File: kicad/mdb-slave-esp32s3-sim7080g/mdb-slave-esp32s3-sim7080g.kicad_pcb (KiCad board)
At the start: 2 copper layers, 58.4 x 41 mm, 56 parts, among them J1 MDB_Connector, J2 USB_C_Receptacle_USB2.0_16P, J3 Conn_02x11_Odd_Even, J4 JAE_SIM_Card_SF72S006, J5 Conn_Coaxial, J6 Conn_Coaxial, SW1 SW_Push, U1 TLP785, U2 SIM7080G, U3 ESP32-S3FH4R2, U4 TLP785, U5 LM2594HVM-3.3, Y1 Crystal_GND24

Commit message: UPdating references
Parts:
- removed AE2: Antenna, RF_Antenna:Johanson_2450AT43F0100
- removed the C4 at (180.2, 90.9)
- removed the D2 at (236.0, 107.1)
- removed the J6 at (240.5, 92.2)
- removed the R1 at (230.6, 110.5)
- added C1: 1.8pf, Capacitor_SMD:C_0603_1608Metric, F.Cu at (235.5, 119.6)
- added C2: NC, Capacitor_SMD:C_0603_1608Metric, F.Cu at (235.5, 122.1)
- added D3: LED, LED_SMD:LED_0603_1608Metric, F.Cu at (247.6, 128.8)
- added J5: Conn_Coaxial, Connector_Coaxial:U.FL_Hirose_U.FL-R-SMT-1_Vertical, F.Cu at (248.1, 121.4)
- added Q1: NPN, Package_TO_SOT_SMD:SOT-23, F.Cu at (231.1, 120.6)
- added Q2: NPN, Package_TO_SOT_SMD:SOT-23, F.Cu at (231.1, 125.0)
- added Q3: NPN, Package_TO_SOT_SMD:SOT-23, F.Cu at (231.1, 129.5)
- added R12: 22ohm, Resistor_SMD:R_0603_1608Metric, F.Cu at (243.6, 119.6)
- added R13: 22ohm, Resistor_SMD:R_0603_1608Metric, F.Cu at (243.6, 122.1)
- added R14: 22ohm, Resistor_SMD:R_0603_1608Metric, F.Cu at (243.6, 124.6)
- added R15: 1k, Resistor_SMD:R_0603_1608Metric, F.Cu at (243.6, 127.2)
- added R2: 10K, Resistor_SMD:R_0603_1608Metric, F.Cu at (239.5, 119.6)
- added R3: 10K, Resistor_SMD:R_0603_1608Metric, F.Cu at (239.5, 122.1)
- added R4: 4K7, Resistor_SMD:R_0603_1608Metric, F.Cu at (239.5, 124.6)
- added R5: 4K7, Resistor_SMD:R_0603_1608Metric, F.Cu at (239.5, 127.2)
- added R6: 4K7, Resistor_SMD:R_0603_1608Metric, F.Cu at (239.5, 129.7)
- added TP3: TestPoint, TestPoint:TestPoint_Pad_D1.0mm, F.Cu at (247.1, 125.9)
- C18: renamed from C19; value 1.8pf -> 27pf
- C19: renamed from C18; value 1.8pf -> 27pf
- C20: value 1.8pf -> NC
- C21: renamed from C17; value 1.8pf -> NC
- L3, L4: value 2.4nh -> 47nh
- moved L1 63.2 mm to (235.5, 124.6)
- moved L3 22.2 mm to (235.5, 127.2)
- moved L4 22.2 mm to (235.5, 129.7)
- moved AE1 0.42 mm to (180.6, 88.7)
- renumbered C7 to C10, C14 to C11, C16 to C12, C15 to C13, C12 to C14, C3 to C15, C13 to C16, C2 to C17, C1 to C3, C5 to C4, C6 to C5, C11 to C6, C8 to C7, C9 to C8, C10 to C9, D5 to D1, D4 to D2, D1 to D4, J2 to J1, J4 to J2, J5 to J4, J1 to J6, R3 to R1, R7 to R10, R8 to R11, R2 to R16, R10 to R17, R5 to R18, R9 to R7, R4 to R8, R6 to R9, TP4 to TP1, TP1 to TP2, U3 to U1, U5 to U3, U1 to U5
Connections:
- C18 pad 2: Net-(J5-In) -> Net-(J4-In)
- C19 pad 2: Net-(AE2-A) -> Net-(J5-In)
- J2 pad C2: /sim_rst -> Net-(J2-RST)
- J2 pad C3: /sim_clk -> Net-(J2-CLK)
- J2 pad C7: /sim_data -> Net-(J2-I/O)
- J4 pad 1: Net-(J5-In) -> Net-(J4-In)
- L1 pad 2: GND -> Net-(U1-LNA_IN/RF)
- L3 pad 1: Net-(AE2-A) -> Net-(J4-In)
- L3 pad 2: /rf_ant -> /gnss_ant
- L4 pad 2: /gnss_ant -> /rf_ant
- U1 pad 1: Net-(U3-LNA_IN/RF) -> Net-(U1-LNA_IN/RF)
- U2 pad 1: /io18 -> /sim_uart1_tx
- U2 pad 2: /io17 -> /sim_uart1_rx
- U2 pad 39: /io14 -> /pwrkey
- U2 pad 40: unconnected-(U2-VDD_EXT-Pad40) -> /sim_vdd_ext

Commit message: Initial organization
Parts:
- removed D3: LED, LED_SMD:LED_0603_1608Metric
- removed R15: 1k, Resistor_SMD:R_0603_1608Metric
- added TP4: TestPoint, TestPoint:TestPoint_Pad_D1.0mm, F.Cu at (206.0, 113.7)
- moved L1 62.7 mm to (182.2, 91.6)
- moved C1 61.0 mm to (182.2, 90.0), turned to 180 degrees
- moved C2 60.7 mm to (182.2, 93.2)
- moved R6 50.2 mm to (218.0, 84.4), turned to 180 degrees
- moved L3 44.5 mm to (213.1, 88.7)
- moved Q3 44.3 mm to (218.4, 87.0), turned to 180 degrees
- moved R2 40.5 mm to (208.1, 94.1)
- moved R4 40.4 mm to (208.1, 99.3)
- moved TP3 38.9 mm to (210.2, 113.4)
- moved R3 37.3 mm to (208.1, 102.1), turned to 180 degrees
- moved R5 37.2 mm to (208.1, 107.3)
- moved J5 37.2 mm to (230.5, 88.7), turned to 90 degrees
- moved L4 35.8 mm to (230.5, 94.2), turned to -90 degrees
- moved Q1 33.1 mm to (208.1, 96.7)
- moved R13 31.5 mm to (213.6, 112.3), turned to -90 degrees
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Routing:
- removed copper zone on F.Cu, net GND
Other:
- board size 58.4 x 41 mm -> 65 x 40 mm
- board text added: "_rf_"
- board text added: "gnss"

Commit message: PCB routing
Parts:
- added H1: MountingHole, MountingHole:MountingHole_2.1mm, F.Cu at (214.3, 123.1)
- added H2: MountingHole, MountingHole:MountingHole_2.1mm, F.Cu at (233.5, 103.3)
- moved C20 3.23 mm to (213.3, 88.7)
- moved L3 1.69 mm to (213.3, 87.0)
- moved C18 1.62 mm to (213.3, 85.4), turned to 180 degrees
- moved TP4 0.90 mm to (206.8, 113.2)
- moved J5 0.37 mm to (230.4, 88.3)
- moved R18 0.21 mm to (197.7, 107.4)
- moved J4 0.18 mm to (209.5, 88.2)
- moved C4 0.13 mm to (197.0, 97.9)
- moved R17 0.11 mm to (204.1, 107.4)
- moved C14 0.10 mm to (200.2, 97.9)
- moved TP2 0.09 mm to (216.0, 88.8)
- moved D2 0.08 mm to (202.7, 97.9)
- moved C10 0.07 mm to (194.5, 104.0)
- moved R7 0.07 mm to (194.5, 100.8)
- moved R9 0.07 mm to (194.5, 102.4)
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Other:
- board text added: "rf_ant"
- board text removed: "_rf_"

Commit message: Routing goods
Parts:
- moved TP3 2.11 mm to (209.8, 111.3)
- moved C13 1.00 mm to (226.9, 88.0)
- moved C11 1.00 mm to (225.3, 88.0)
- moved C19 0.44 mm to (231.1, 91.5)
- moved C21 0.44 mm to (231.9, 93.8)
- moved L4 0.44 mm to (230.4, 93.8)
- moved TP1 0.24 mm to (210.9, 121.2)
- moved H2 0.21 mm to (233.5, 103.1)
- moved C6 0.12 mm to (187.3, 98.3)
- moved C8 0.11 mm to (189.1, 98.3)
- moved C12 0.10 mm to (222.7, 87.0)
- moved C1 0.08 mm to (182.2, 90.1)
- turned R3 to 0 degrees
- turned R4 to 180 degrees
- turned R5 to 180 degrees
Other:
- board text added: "gps"
- board text removed: "gnss"

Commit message: Routing...
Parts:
- moved TP1 1.47 mm to (211.3, 119.8)
- moved D2 0.08 mm to (202.8, 97.9)
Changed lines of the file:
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@@
 	(footprint "TestPoint:TestPoint_Pad_D1.0mm"
 		(layer "F.Cu")
-		(at 210.89 121.175)
+		(at 211.32 119.77)
 		(descr "SMD pad as test Point, diameter 1.0mm")
 		(tags "test point SMD pad")
@@
 	(footprint "LED_SMD:LED_WS2812B-2020_PLCC4_2.0x2.0mm"
 		(layer "F.Cu")
-		(at 202.700666 97.885)
+		(at 202.776667 97.885)
 		(descr "2.0mm x 2.0mm Addressable RGB LED NeoPixel Nano, 12 mA, https://cdn-shop.adafruit.com/product-files/4684/4684_WS2812B-2020_V1.3_EN.pdf")
 		(tags "LED RGB NeoPixel Nano PLCC-4 2020")

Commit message: Routing
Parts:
- moved C16 16.3 mm to (230.2, 109.5), turned to 0 degrees
- moved TP4 1.56 mm to (205.9, 111.9)
- moved TP1 1.16 mm to (210.9, 118.7)
- moved TP3 1.14 mm to (210.1, 110.2)
- moved R17 0.62 mm to (203.5, 107.4), turned to -90 degrees
- moved J6 0.25 mm to (187.5, 86.2)
- moved J2 0.23 mm to (227.9, 117.5)
- moved R13 0.13 mm to (213.8, 112.3)
- moved R12 0.13 mm to (215.5, 112.3)
- moved R14 0.13 mm to (217.2, 112.3)
- moved C14 0.11 mm to (200.3, 97.9)
- moved R16 0.06 mm to (201.0, 107.4)
- turned C15 to 90 degrees
- turned R2 to 180 degrees
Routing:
- net GND: track 0.00 -> 425.8 mm, vias 0 -> 7
- net +3V3: track 0.00 -> 153.4 mm, vias 0 -> 9
- net /vin: track 0.00 -> 98.9 mm, vias 0 -> 2
- net /io21: track 0.00 -> 57.0 mm, vias 0 -> 2
- net /io14: track 0.00 -> 54.3 mm, vias 0 -> 2
- net /boot: track 0.00 -> 52.4 mm
- net /io18: track 0.00 -> 50.5 mm, vias 0 -> 2
- net /io4: track 0.00 -> 47.3 mm, vias 0 -> 2
- net /io17: track 0.00 -> 41.6 mm, vias 0 -> 2
- net /io5: track 0.00 -> 35.7 mm, vias 0 -> 2
- net /mdb_communications_common: track 0.00 -> 30.1 mm
- net /sim_vdd_ext: track 0.00 -> 27.7 mm, vias 0 -> 2
- net /mdb_master_receive: track 0.00 -> 26.3 mm
- net /u0txd: track 0.00 -> 25.7 mm, vias 0 -> 1
- net /u0rxd: track 0.00 -> 22.2 mm, vias 0 -> 1
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
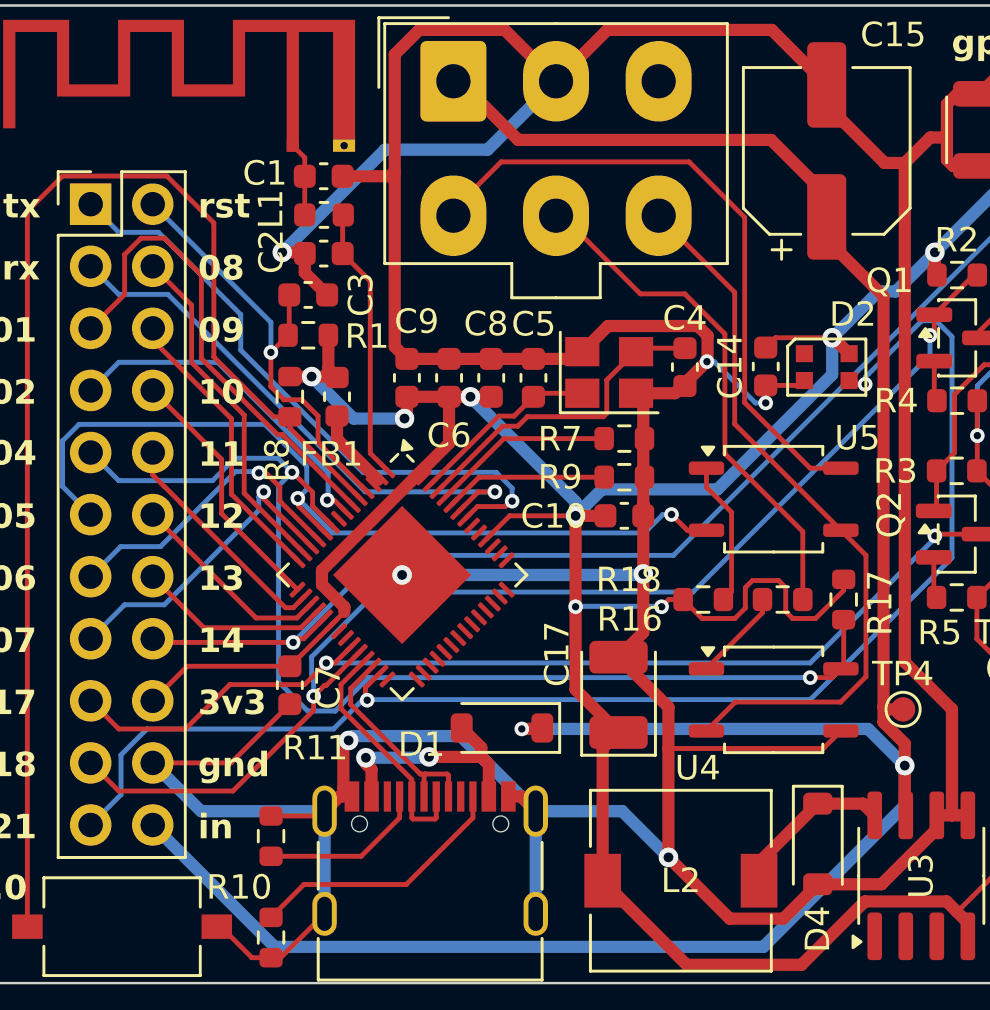
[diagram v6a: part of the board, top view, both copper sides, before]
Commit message: Refacting production components
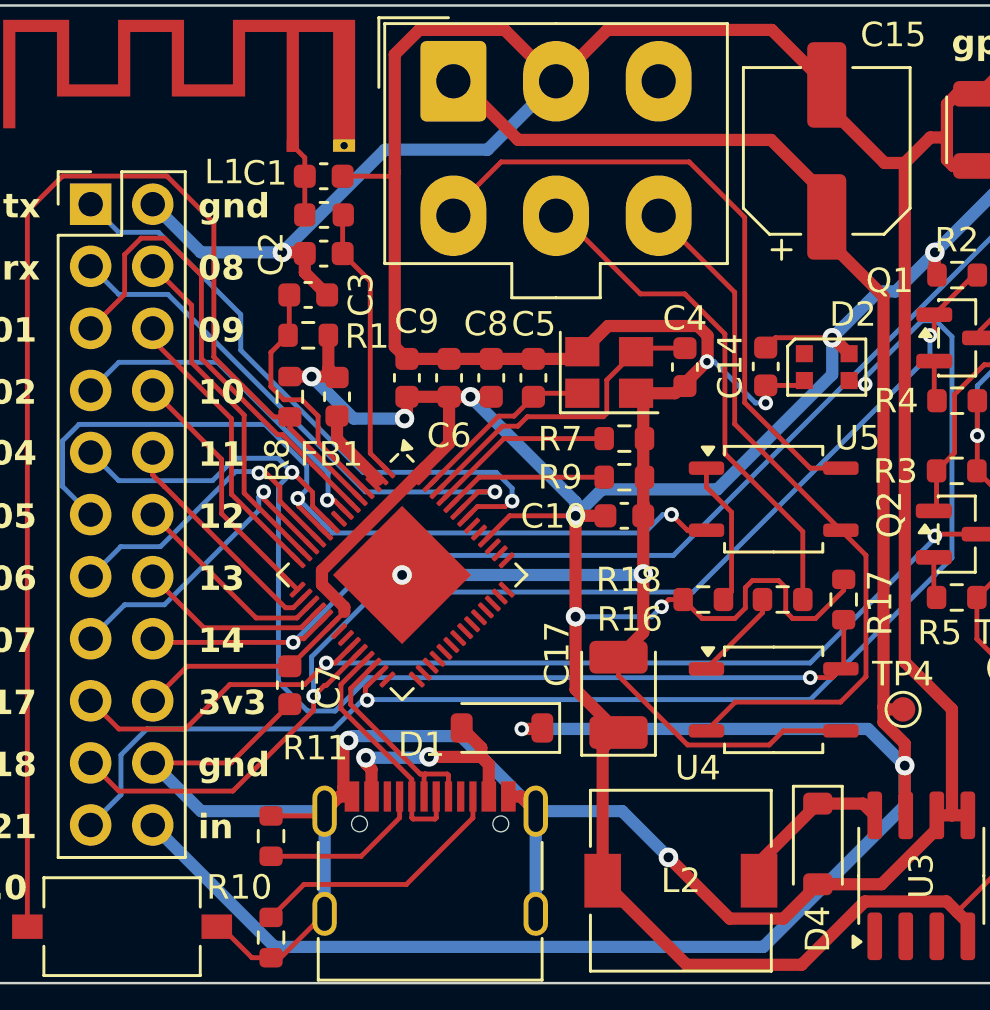
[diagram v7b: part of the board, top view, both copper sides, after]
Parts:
- added REF**: OSHW-Logo2_14.6x12mm_SilkScreen, Symbol:OSHW-Logo2_14.6x12mm_SilkScreen, B.Cu at (223.5, 114.2)
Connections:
- C3 pad 1: /reset -> Net-(U1-CHIP_PU/RESET)
- J3 pad 2: /reset -> GND
- R1 pad 2: /reset -> Net-(U1-CHIP_PU/RESET)
- U1 pad 4: /reset -> Net-(U1-CHIP_PU/RESET)
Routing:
- net /reset: track 18.5 -> 0.00 mm, vias 1 -> 0
- net Net-(U1-CHIP_PU/RESET): track 0.00 -> 10.4 mm
- net GND: track 425.8 -> 426.8 mm
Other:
- board text added: "mdb-target-esp32s3-sim7080g"
- board text removed: "mdb-target-esp32s3"
- board text removed: "rst"

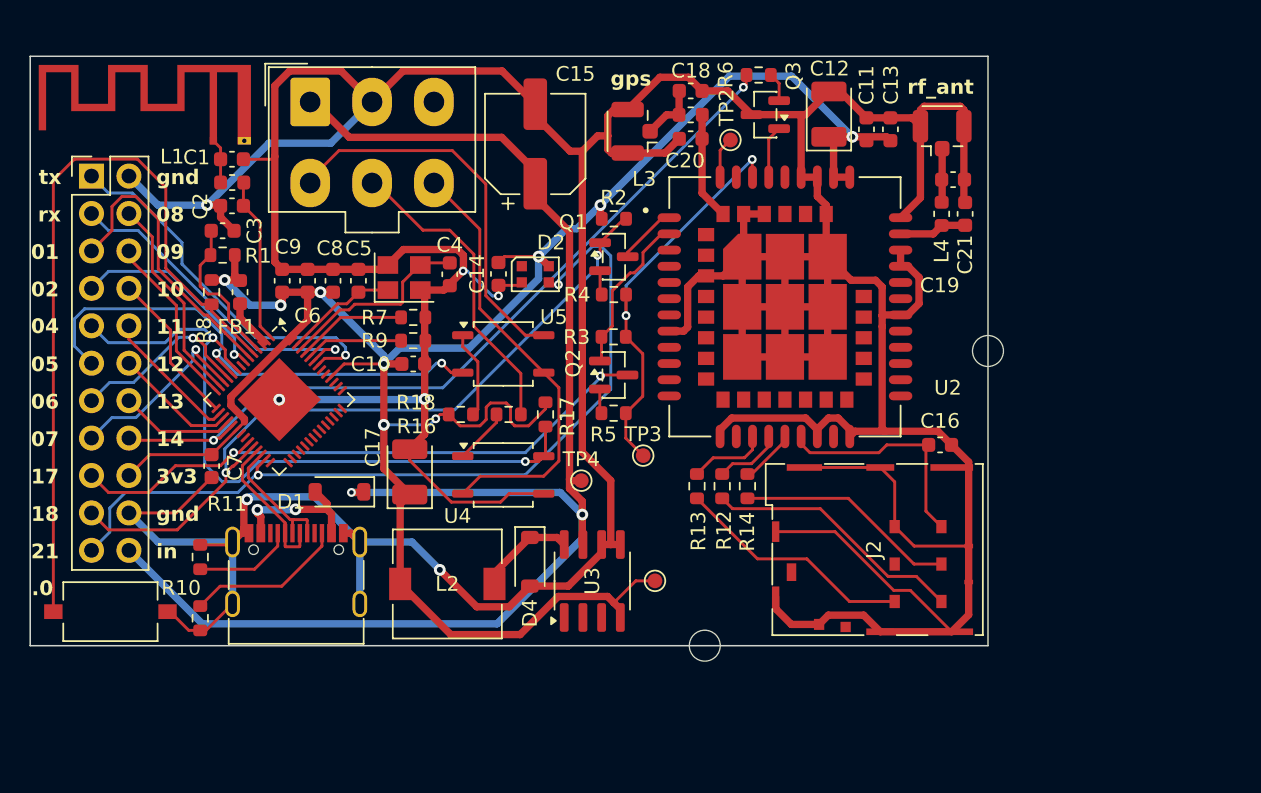
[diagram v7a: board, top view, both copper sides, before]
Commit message: updating production components
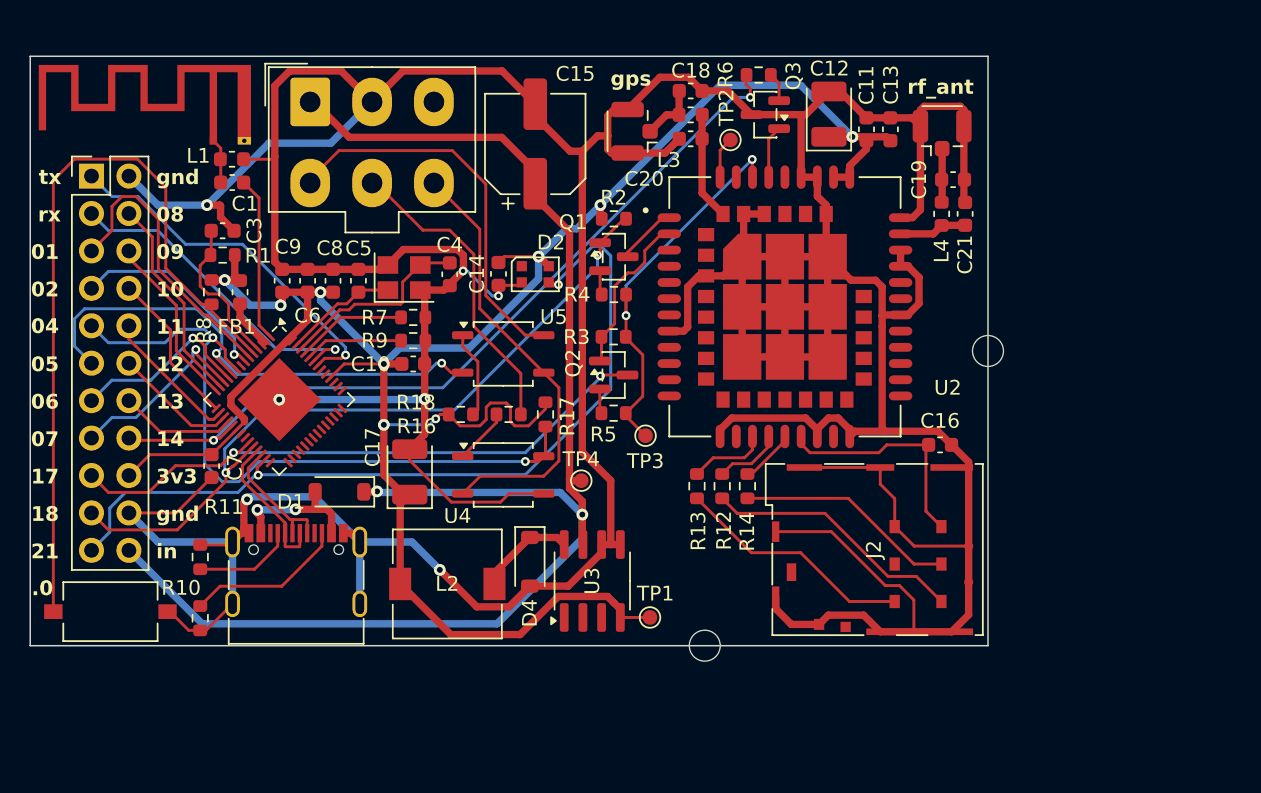
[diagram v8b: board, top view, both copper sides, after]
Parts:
- removed C2: NC, Capacitor_SMD:C_0603_1608Metric
- removed REF**: OSHW-Logo2_14.6x12mm_SilkScreen, Symbol:OSHW-Logo2_14.6x12mm_SilkScreen
- moved TP1 2.51 mm to (210.6, 121.2)
- moved C1 1.58 mm to (182.2, 91.7), turned to 0 degrees
- moved L1 1.58 mm to (182.2, 90.1), turned to 180 degrees
- moved TP3 1.36 mm to (210.3, 108.8)
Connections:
- C1 pad 1: GND -> Net-(AE1-A)
- C1 pad 2: Net-(AE1-A) -> Net-(U1-LNA_IN/RF)
- L1 pad 1: Net-(AE1-A) -> GND
- L1 pad 2: Net-(U1-LNA_IN/RF) -> Net-(AE1-A)
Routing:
- net /vin: track 98.9 -> 97.2 mm
- net /sim_vdd_ext: track 27.7 -> 26.5 mm
- net +3V3: track 153.6 -> 152.4 mm
- net /io14: track 54.3 -> 55.3 mm
- net /u0txd: track 25.7 -> 24.8 mm
- net GND: track 426.8 -> 425.9 mm
